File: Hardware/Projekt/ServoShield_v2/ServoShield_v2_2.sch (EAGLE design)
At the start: 60 parts, among them IC1 ATMEGA644A, Q1 8MHz

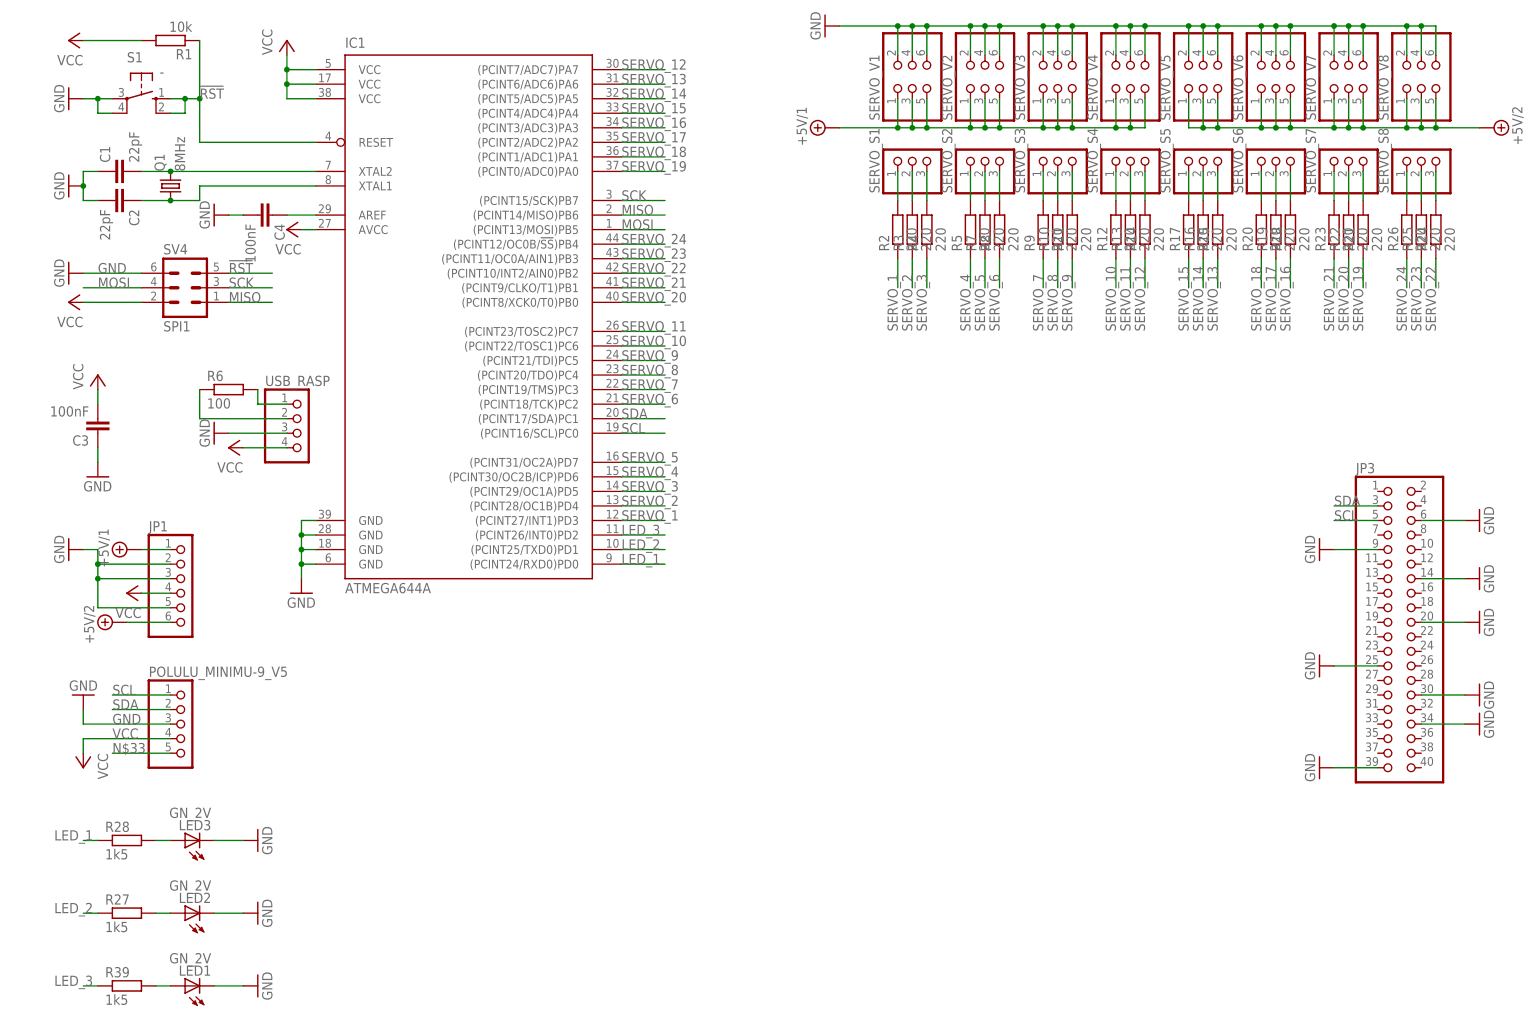
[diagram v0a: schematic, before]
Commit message: Added connectors for power and finished routing
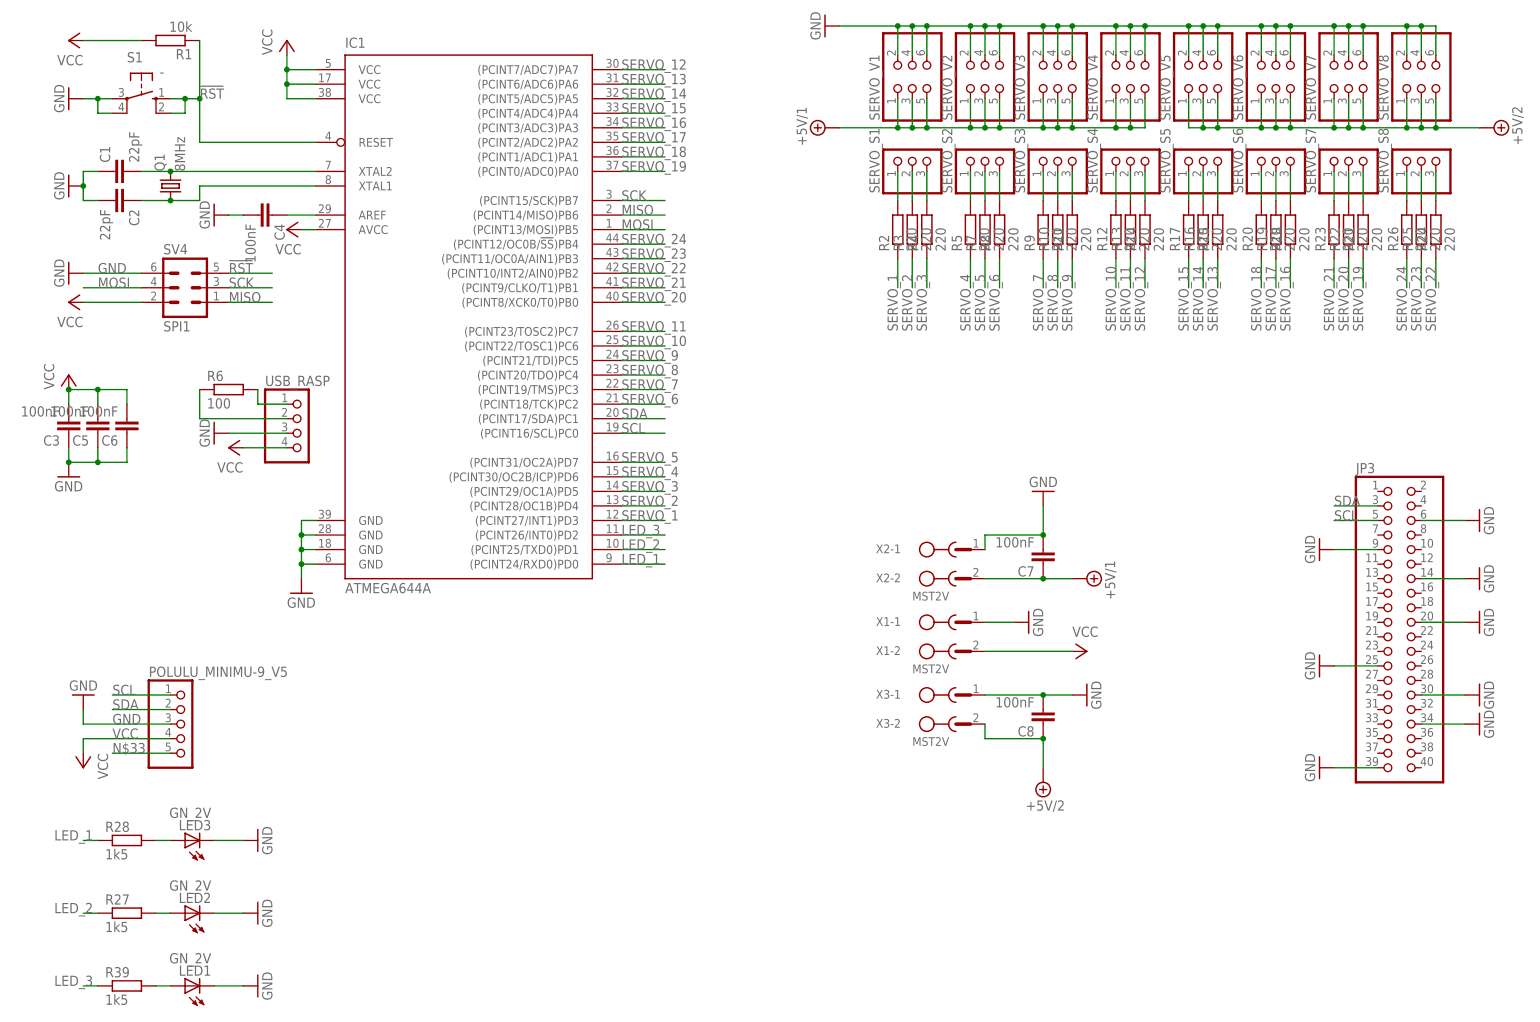
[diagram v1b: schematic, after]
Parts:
- removed JP1: (no value), pinhead:PINHD-1X6
- added C5, C6, C7, C8: 100nF, resistor:C-EUC0805
- added X1, X2, X3: MST2V, PHO508E:MST2V
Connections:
- net +5V/1: now also C7.1, X2-2.1; no longer JP1.1
- net +5V/2: now also C8.1, X3-2.1; no longer JP1.6
- net GND: now also C5.1, C6.1, C7.2, C8.2, X1-1.1, X2-1.1, X3-1.1; no longer JP1.2, JP1.3, JP1.5
- net VCC: now also C5.2, C6.2, X1-2.1; no longer JP1.4
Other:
- moved on the sheet: C3
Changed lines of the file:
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@@
 <part name="P+3" library="supply1" deviceset="VCC" device=""/>
 <part name="P+2" library="supply1" deviceset="VCC" device=""/>
-<part name="JP1" library="pinhead" deviceset="PINHD-1X6" device=""/>
-<part name="SUPPLY3" library="supply2" deviceset="+5V/1" device=""/>
-<part name="SUPPLY4" library="supply2" deviceset="+5V/2" device=""/>
-<part name="P+5" library="supply1" deviceset="VCC" device=""/>
-<part name="GND7" library="supply1" deviceset="GND" device=""/>
 <part name="USB_RASP" library="pinhead" deviceset="PINHD-1X4" device=""/>
 <part name="P+6" library="supply1" deviceset="VCC" device=""/>
@@
 <part name="C4" library="resistor" deviceset="C-EU" device="C0805" value="100nF"/>
 <part name="GND21" library="supply1" deviceset="GND" device=""/>
+<part name="X2" library="PHO508E" deviceset="MST2V" device="" value="MST2V"/>
+<part name="X1" library="PHO508E" deviceset="MST2V" device="" value="MST2V"/>
+<part name="X3" library="PHO508E" deviceset="MST2V" device="" value="MST2V"/>
+<part name="SUPPLY5" library="supply2" deviceset="+5V/1" device=""/>
+<part name="SUPPLY6" library="supply2" deviceset="+5V/2" device=""/>
+<part name="P+9" library="supply1" deviceset="VCC" device=""/>
+<part name="GND22" library="supply1" deviceset="GND" device=""/>
+<part name="GND23" library="supply1" deviceset="GND" device=""/>
+<part name="GND24" library="supply1" deviceset="GND" device=""/>
+<part name="C5" library="resistor" deviceset="C-EU" device="C0805" value="100nF"/>
+<part name="C6" library="resistor" deviceset="C-EU" device="C0805" value="100nF"/>
+<part name="C7" library="resistor" deviceset="C-EU" device="C0805" value="100nF"/>
+<part name="C8" library="resistor" deviceset="C-EU" device="C0805" value="100nF"/>
 </parts>
 <sheets>
@@
 <instance part="C2" gate="G$1" x="15.24" y="147.32" rot="R270"/>
 <instance part="GND1" gate="1" x="5.08" y="149.86" rot="R270"/>
-<instance part="GND2" gate="1" x="10.16" y="99.06"/>
+<instance part="GND2" gate="1" x="5.08" y="99.06"/>
 <instance part="R1" gate="G$1" x="22.86" y="175.26" rot="R180"/>
 <instance part="S1" gate="1" x="17.78" y="165.1" rot="R270"/>
@@
 <instance part="SV4" gate="1" x="25.4" y="132.08"/>
 <instance part="GND5" gate="1" x="5.08" y="134.62" rot="R270"/>
-<instance part="C3" gate="G$1" x="10.16" y="106.68" rot="R180"/>
-<instance part="P+1" gate="VCC" x="10.16" y="116.84"/>
+<instance part="C3" gate="G$1" x="5.08" y="106.68" rot="R180"/>
+<instance part="P+1" gate="VCC" x="5.08" y="116.84"/>
 <instance part="P+3" gate="VCC" x="5.08" y="129.54" rot="R90"/>
 <instance part="P+2" gate="VCC" x="5.08" y="175.26" rot="R90"/>
-<instance part="JP1" gate="A" x="25.4" y="78.74"/>
-<instance part="SUPPLY3" gate="G$1" x="15.24" y="86.36" rot="R90"/>
-<instance part="SUPPLY4" gate="G$1" x="12.7" y="73.66" rot="R90"/>
-<instance part="P+5" gate="VCC" x="15.24" y="78.74" rot="R90"/>
-<instance part="GND7" gate="1" x="5.08" y="86.36" rot="R270"/>
 <instance part="USB_RASP" gate="A" x="45.72" y="106.68"/>
 <instance part="P+6" gate="VCC" x="33.02" y="104.14" rot="R90"/>
@@
 <instance part="C4" gate="G$1" x="40.64" y="144.78" rot="R270"/>
 <instance part="GND21" gate="1" x="30.48" y="144.78" rot="R270"/>
+<instance part="X2" gate="-1" x="160.02" y="86.36"/>
+<instance part="X2" gate="-2" x="160.02" y="81.28"/>
+<instance part="X1" gate="-1" x="160.02" y="73.66"/>
+<instance part="X1" gate="-2" x="160.02" y="68.58"/>
+<instance part="X3" gate="-1" x="160.02" y="60.96"/>
+<instance part="X3" gate="-2" x="160.02" y="55.88"/>
+<instance part="SUPPLY5" gate="G$1" x="182.88" y="81.28" rot="R270"/>
+<instance part="SUPPLY6" gate="G$1" x="175.26" y="45.72" rot="R180"/>
+<instance part="P+9" gate="VCC" x="182.88" y="68.58" rot="R270"/>
+<instance part="GND22" gate="1" x="172.72" y="73.66" rot="R90"/>
+<instance part="GND23" gate="1" x="175.26" y="96.52" rot="R180"/>
+<instance part="GND24" gate="1" x="182.88" y="60.96" rot="R90"/>
+<instance part="C5" gate="G$1" x="10.16" y="106.68" rot="R180"/>
+<instance part="C6" gate="G$1" x="15.24" y="106.68" rot="R180"/>
+<instance part="C7" gate="G$1" x="175.26" y="83.82" rot="R180"/>
+<instance part="C8" gate="G$1" x="175.26" y="55.88" rot="R180"/>
 </instances>
 <busses>
@@
 <pinref part="GND2" gate="1" pin="GND"/>
 <pinref part="C3" gate="G$1" pin="1"/>
-<wire x1="10.16" y1="101.6" x2="10.16" y2="104.14" width="0.1524" layer="91"/>
+<wire x1="5.08" y1="101.6" x2="5.08" y2="104.14" width="0.1524" layer="91"/>
+<pinref part="C5" gate="G$1" pin="1"/>
+<wire x1="10.16" y1="104.14" x2="10.16" y2="101.6" width="0.1524" layer="91"/>
+<wire x1="10.16" y1="101.6" x2="5.08" y2="101.6" width="0.1524" layer="91"/>
+<junction x="5.08" y="101.6"/>
+<pinref part="C6" gate="G$1" pin="1"/>
+<wire x1="15.24" y1="104.14" x2="15.24" y2="101.6" width="0.1524" layer="91"/>
+<wire x1="15.24" y1="101.6" x2="10.16" y2="101.6" width="0.1524" layer="91"/>
+<junction x="10.16" y="101.6"/>
 </segment>
 <segment>
@@
 <pinref part="USB_RASP" gate="A" pin="3"/>
 <wire x1="33.02" y1="106.68" x2="43.18" y2="106.68" width="0.1524" layer="91"/>
-</segment>
-<segment>
-<pinref part="JP1" gate="A" pin="5"/>
-<pinref part="GND7" gate="1" pin="GND"/>
-<wire x1="22.86" y1="76.2" x2="10.16" y2="76.2" width="0.1524" layer="91"/>
-<wire x1="10.16" y1="76.2" x2="10.16" y2="81.28" width="0.1524" layer="91"/>
-<pinref part="JP1" gate="A" pin="3"/>
-<wire x1="10.16" y1="81.28" x2="10.16" y2="83.82" width="0.1524" layer="91"/>
-<wire x1="10.16" y1="83.82" x2="10.16" y2="86.36" width="0.1524" layer="91"/>
-<wire x1="10.16" y1="86.36" x2="7.62" y2="86.36" width="0.1524" layer="91"/>
-<wire x1="22.86" y1="81.28" x2="10.16" y2="81.28" width="0.1524" layer="91"/>
-<junction x="10.16" y="81.28"/>
-<pinref part="JP1" gate="A" pin="2"/>
-<wire x1="22.86" y1="83.82" x2="10.16" y2="83.82" width="0.1524" layer="91"/>
-<junction x="10.16" y="83.82"/>
 </segment>
 <segment>
@@
 <wire x1="33.02" y1="144.78" x2="35.56" y2="144.78" width="0.1524" layer="91"/>
 </segment>
+<segment>
+<pinref part="X1" gate="-1" pin="1"/>
+<pinref part="GND22" gate="1" pin="GND"/>
+<wire x1="165.1" y1="73.66" x2="170.18" y2="73.66" width="0.1524" layer="91"/>
+</segment>
+<segment>
+<pinref part="X3" gate="-1" pin="1"/>
+<pinref part="GND24" gate="1" pin="GND"/>
+<wire x1="165.1" y1="60.96" x2="175.26" y2="60.96" width="0.1524" layer="91"/>
+<pinref part="C8" gate="G$1" pin="2"/>
+<wire x1="175.26" y1="60.96" x2="180.34" y2="60.96" width="0.1524" layer="91"/>
+<junction x="175.26" y="60.96"/>
+</segment>
+<segment>
+<pinref part="C7" gate="G$1" pin="2"/>
+<wire x1="175.26" y1="88.9" x2="165.1" y2="88.9" width="0.1524" layer="91"/>
+<pinref part="X2" gate="-1" pin="1"/>
+<wire x1="165.1" y1="88.9" x2="165.1" y2="86.36" width="0.1524" layer="91"/>
+<pinref part="GND23" gate="1" pin="GND"/>
+<wire x1="175.26" y1="93.98" x2="175.26" y2="88.9" width="0.1524" layer="91"/>
+<junction x="175.26" y="88.9"/>
+</segment>
 </net>
 <net name="N$2" class="0">
@@
 <segment>
 <pinref part="C3" gate="G$1" pin="2"/>
+<wire x1="5.08" y1="111.76" x2="5.08" y2="114.3" width="0.1524" layer="91"/>
+<pinref part="P+1" gate="VCC" pin="VCC"/>
+<pinref part="C5" gate="G$1" pin="2"/>
 <wire x1="10.16" y1="111.76" x2="10.16" y2="114.3" width="0.1524" layer="91"/>
-<pinref part="P+1" gate="VCC" pin="VCC"/>
+<wire x1="10.16" y1="114.3" x2="5.08" y2="114.3" width="0.1524" layer="91"/>
+<junction x="5.08" y="114.3"/>
+<pinref part="C6" gate="G$1" pin="2"/>
+<wire x1="15.24" y1="111.76" x2="15.24" y2="114.3" width="0.1524" layer="91"/>
+<wire x1="15.24" y1="114.3" x2="10.16" y2="114.3" width="0.1524" layer="91"/>
+<junction x="10.16" y="114.3"/>
 </segment>
 <segment>
@@
 <wire x1="17.78" y1="175.26" x2="7.62" y2="175.26" width="0.1524" layer="91"/>
 <pinref part="P+2" gate="VCC" pin="VCC"/>
-</segment>
-<segment>
-<pinref part="P+5" gate="VCC" pin="VCC"/>
-<pinref part="JP1" gate="A" pin="4"/>
-<wire x1="17.78" y1="78.74" x2="22.86" y2="78.74" width="0.1524" layer="91"/>
 </segment>
 <segment>
@@
 <pinref part="P+8" gate="VCC" pin="VCC"/>
 <wire x1="48.26" y1="142.24" x2="45.72" y2="142.24" width="0.1524" layer="91"/>
+</segment>
+<segment>
+<pinref part="X1" gate="-2" pin="1"/>
+<pinref part="P+9" gate="VCC" pin="VCC"/>
+<wire x1="165.1" y1="68.58" x2="180.34" y2="68.58" width="0.1524" layer="91"/>
 </segment>
 </net>
@@
 </segment>
 <segment>
-<pinref part="JP1" gate="A" pin="1"/>
-<pinref part="SUPPLY3" gate="G$1" pin="+5V/1"/>
-<wire x1="22.86" y1="86.36" x2="17.78" y2="86.36" width="0.1524" layer="91"/>
+<pinref part="X2" gate="-2" pin="1"/>
+<pinref part="SUPPLY5" gate="G$1" pin="+5V/1"/>
+<wire x1="165.1" y1="81.28" x2="175.26" y2="81.28" width="0.1524" layer="91"/>
+<pinref part="C7" gate="G$1" pin="1"/>
+<wire x1="175.26" y1="81.28" x2="180.34" y2="81.28" width="0.1524" layer="91"/>
+<junction x="175.26" y="81.28"/>
 </segment>
 </net>
@@
 </segment>
 <segment>
-<pinref part="JP1" gate="A" pin="6"/>
-<pinref part="SUPPLY4" gate="G$1" pin="+5V/2"/>
-<wire x1="22.86" y1="73.66" x2="15.24" y2="73.66" width="0.1524" layer="91"/>
-</segment>
-</net>
+<pinref part="X3" gate="-2" pin="1"/>
+<wire x1="165.1" y1="55.88" x2="165.1" y2="53.34" width="0.1524" layer="91"/>
+<pinref part="C8" gate="G$1" pin="1"/>
+<wire x1="165.1" y1="53.34" x2="175.26" y2="53.34" width="0.1524" layer="91"/>
+<pinref part="SUPPLY6" gate="G$1" pin="+5V/2"/>
+<wire x1="175.26" y1="48.26" x2="175.26" y2="53.34" width="0.1524" layer="91"/>
+<junction x="175.26" y="53.34"/>
+</segment>
+</net>

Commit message: Minor changes
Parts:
- removed C7, C8: 100nF, resistor:C-EUC0805
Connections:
- net +5V/1: no longer C7.1
- net +5V/2: no longer C8.1
- net GND: no longer C7.2, C8.2
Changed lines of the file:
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@@
 <part name="C5" library="resistor" deviceset="C-EU" device="C0805" value="100nF"/>
 <part name="C6" library="resistor" deviceset="C-EU" device="C0805" value="100nF"/>
-<part name="C7" library="resistor" deviceset="C-EU" device="C0805" value="100nF"/>
-<part name="C8" library="resistor" deviceset="C-EU" device="C0805" value="100nF"/>
 </parts>
 <sheets>
@@
 <instance part="X3" gate="-2" x="160.02" y="55.88"/>
 <instance part="SUPPLY5" gate="G$1" x="182.88" y="81.28" rot="R270"/>
-<instance part="SUPPLY6" gate="G$1" x="175.26" y="45.72" rot="R180"/>
+<instance part="SUPPLY6" gate="G$1" x="182.88" y="55.88" rot="R270"/>
 <instance part="P+9" gate="VCC" x="182.88" y="68.58" rot="R270"/>
 <instance part="GND22" gate="1" x="172.72" y="73.66" rot="R90"/>
-<instance part="GND23" gate="1" x="175.26" y="96.52" rot="R180"/>
+<instance part="GND23" gate="1" x="182.88" y="86.36" rot="R90"/>
 <instance part="GND24" gate="1" x="182.88" y="60.96" rot="R90"/>
 <instance part="C5" gate="G$1" x="10.16" y="106.68" rot="R180"/>
 <instance part="C6" gate="G$1" x="15.24" y="106.68" rot="R180"/>
-<instance part="C7" gate="G$1" x="175.26" y="83.82" rot="R180"/>
-<instance part="C8" gate="G$1" x="175.26" y="55.88" rot="R180"/>
 </instances>
 <busses>
@@
 <pinref part="X3" gate="-1" pin="1"/>
 <pinref part="GND24" gate="1" pin="GND"/>
-<wire x1="165.1" y1="60.96" x2="175.26" y2="60.96" width="0.1524" layer="91"/>
-<pinref part="C8" gate="G$1" pin="2"/>
-<wire x1="175.26" y1="60.96" x2="180.34" y2="60.96" width="0.1524" layer="91"/>
-<junction x="175.26" y="60.96"/>
-</segment>
-<segment>
-<pinref part="C7" gate="G$1" pin="2"/>
-<wire x1="175.26" y1="88.9" x2="165.1" y2="88.9" width="0.1524" layer="91"/>
+<wire x1="165.1" y1="60.96" x2="180.34" y2="60.96" width="0.1524" layer="91"/>
+</segment>
+<segment>
+<wire x1="180.34" y1="86.36" x2="165.1" y2="86.36" width="0.1524" layer="91"/>
 <pinref part="X2" gate="-1" pin="1"/>
-<wire x1="165.1" y1="88.9" x2="165.1" y2="86.36" width="0.1524" layer="91"/>
 <pinref part="GND23" gate="1" pin="GND"/>
-<wire x1="175.26" y1="93.98" x2="175.26" y2="88.9" width="0.1524" layer="91"/>
-<junction x="175.26" y="88.9"/>
 </segment>
 </net>
@@
 <pinref part="X2" gate="-2" pin="1"/>
 <pinref part="SUPPLY5" gate="G$1" pin="+5V/1"/>
-<wire x1="165.1" y1="81.28" x2="175.26" y2="81.28" width="0.1524" layer="91"/>
-<pinref part="C7" gate="G$1" pin="1"/>
-<wire x1="175.26" y1="81.28" x2="180.34" y2="81.28" width="0.1524" layer="91"/>
-<junction x="175.26" y="81.28"/>
+<wire x1="165.1" y1="81.28" x2="180.34" y2="81.28" width="0.1524" layer="91"/>
 </segment>
 </net>
@@
 <segment>
 <pinref part="X3" gate="-2" pin="1"/>
-<wire x1="165.1" y1="55.88" x2="165.1" y2="53.34" width="0.1524" layer="91"/>
-<pinref part="C8" gate="G$1" pin="1"/>
-<wire x1="165.1" y1="53.34" x2="175.26" y2="53.34" width="0.1524" layer="91"/>
+<wire x1="165.1" y1="55.88" x2="180.34" y2="55.88" width="0.1524" layer="91"/>
 <pinref part="SUPPLY6" gate="G$1" pin="+5V/2"/>
-<wire x1="175.26" y1="48.26" x2="175.26" y2="53.34" width="0.1524" layer="91"/>
-<junction x="175.26" y="53.34"/>
-</segment>
-</net>
+</segment>
+</net>
